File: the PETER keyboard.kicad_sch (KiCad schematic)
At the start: 140 parts

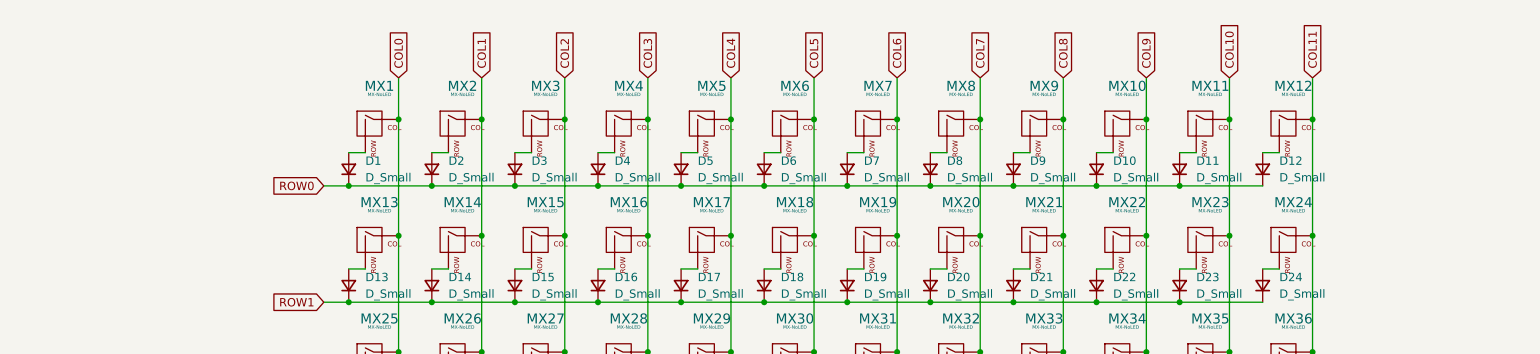
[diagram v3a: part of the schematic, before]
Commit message: added first draft of rotary encoders
not confirmed to work
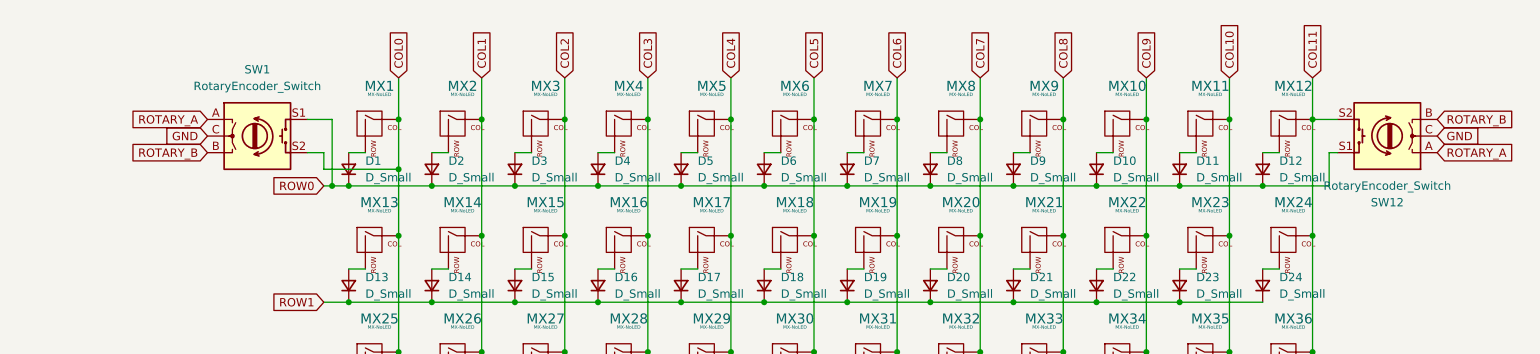
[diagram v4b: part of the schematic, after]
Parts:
- added SW1, SW12: RotaryEncoder_Switch, symbol Device:RotaryEncoder_Switch
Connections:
- net COL0: now also SW1.S2
- net COL11: now also SW12.S2
- net GND: now also SW1.C, SW12.C
- net ROW0: now also SW1.S1, SW12.S1
- new net ROTARY_A: SW1.A, SW12.A
- new net ROTARY_B: SW1.B, SW12.B
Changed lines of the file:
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@@
   (junction (at 240.03 25.4) (diameter 0) (color 0 0 0 0)
   )
+  (junction (at 102.87 35.56) (diameter 0) (color 0 0 0 0)
+  )
   (junction (at 25.4 114.3) (diameter 0) (color 0 0 0 0)
   )
@@
   (junction (at 219.71 106.68) (diameter 0) (color 0 0 0 0)
   )
+  (junction (at 113.03 33.02) (diameter 0) (color 0 0 0 0)
+  )
   (junction (at 105.41 71.12) (diameter 0) (color 0 0 0 0)
   )
@@
   (junction (at 105.41 35.56) (diameter 0) (color 0 0 0 0)
   )
+  (junction (at 245.11 35.56) (diameter 0) (color 0 0 0 0)
+  )
   (junction (at 118.11 53.34) (diameter 0) (color 0 0 0 0)
   )
@@
     (stroke (width 0) (type default) (color 0 0 0 0))
   )
+  (wire (pts (xy 255.27 30.48) (xy 255.27 35.56))
+    (stroke (width 0) (type default) (color 0 0 0 0))
+  )
   (wire (pts (xy 93.98 175.26) (xy 92.71 175.26))
     (stroke (width 0) (type default) (color 0 0 0 0))
@@
     (stroke (width 0) (type default) (color 0 0 0 0))
   )
+  (wire (pts (xy 101.6 30.48) (xy 101.6 33.02))
+    (stroke (width 0) (type default) (color 0 0 0 0))
+  )
   (wire (pts (xy 25.4 119.38) (xy 35.56 119.38))
     (stroke (width 0) (type default) (color 0 0 0 0))
@@
     (stroke (width 0) (type default) (color 0 0 0 0))
   )
+  (wire (pts (xy 102.87 25.4) (xy 102.87 35.56))
+    (stroke (width 0) (type default) (color 0 0 0 0))
+  )
   (wire (pts (xy 118.11 88.9) (xy 130.81 88.9))
     (stroke (width 0) (type default) (color 0 0 0 0))
@@
     (stroke (width 0) (type default) (color 0 0 0 0))
   )
+  (wire (pts (xy 101.6 33.02) (xy 113.03 33.02))
+    (stroke (width 0) (type default) (color 0 0 0 0))
+  )
   (wire (pts (xy 219.71 106.68) (xy 232.41 106.68))
     (stroke (width 0) (type default) (color 0 0 0 0))
@@
     (stroke (width 0) (type default) (color 0 0 0 0))
   )
+  (wire (pts (xy 102.87 35.56) (xy 105.41 35.56))
+    (stroke (width 0) (type default) (color 0 0 0 0))
+  )
   (wire (pts (xy 194.31 48.26) (xy 196.85 48.26))
     (stroke (width 0) (type default) (color 0 0 0 0))
@@
     (stroke (width 0) (type default) (color 0 0 0 0))
   )
+  (wire (pts (xy 113.03 33.02) (xy 113.03 43.18))
+    (stroke (width 0) (type default) (color 0 0 0 0))
+  )
   (wire (pts (xy 214.63 78.74) (xy 214.63 96.52))
     (stroke (width 0) (type default) (color 0 0 0 0))
@@
     (stroke (width 0) (type default) (color 0 0 0 0))
   )
+  (wire (pts (xy 252.73 25.4) (xy 256.54 25.4))
+    (stroke (width 0) (type default) (color 0 0 0 0))
+  )
   (wire (pts (xy 101.6 161.29) (xy 104.14 161.29))
     (stroke (width 0) (type default) (color 0 0 0 0))
@@
     (stroke (width 0) (type default) (color 0 0 0 0))
   )
+  (wire (pts (xy 256.54 30.48) (xy 255.27 30.48))
+    (stroke (width 0) (type default) (color 0 0 0 0))
+  )
   (wire (pts (xy 245.11 48.26) (xy 247.65 48.26))
     (stroke (width 0) (type default) (color 0 0 0 0))
@@
     (stroke (width 0) (type default) (color 0 0 0 0))
   )
-  (wire (pts (xy 101.6 35.56) (xy 105.41 35.56))
+  (wire (pts (xy 101.6 35.56) (xy 102.87 35.56))
     (stroke (width 0) (type default) (color 0 0 0 0))
   )
@@
     (stroke (width 0) (type default) (color 0 0 0 0))
   )
+  (wire (pts (xy 245.11 35.56) (xy 255.27 35.56))
+    (stroke (width 0) (type default) (color 0 0 0 0))
+  )
   (wire (pts (xy 181.61 53.34) (xy 194.31 53.34))
     (stroke (width 0) (type default) (color 0 0 0 0))
@@
     (stroke (width 0) (type default) (color 0 0 0 0))
   )
+  (wire (pts (xy 99.06 30.48) (xy 101.6 30.48))
+    (stroke (width 0) (type default) (color 0 0 0 0))
+  )
   (wire (pts (xy 125.73 43.18) (xy 125.73 60.96))
     (stroke (width 0) (type default) (color 0 0 0 0))
@@
     (stroke (width 0) (type default) (color 0 0 0 0))
   )
-  (wire (pts (xy 113.03 25.4) (xy 113.03 43.18))
+  (wire (pts (xy 113.03 25.4) (xy 113.03 33.02))
     (stroke (width 0) (type default) (color 0 0 0 0))
   )
@@
     (stroke (width 0) (type default) (color 0 0 0 0))
   )
+  (wire (pts (xy 99.06 25.4) (xy 102.87 25.4))
+    (stroke (width 0) (type default) (color 0 0 0 0))
+  )
   (wire (pts (xy 22.86 163.83) (xy 25.4 163.83))
     (stroke (width 0) (type default) (color 0 0 0 0))
@@
     )
   )
+  (global_label "GND" (shape input) (at 271.78 27.94 0) (fields_autoplaced)
+    (effects (font (size 1.27 1.27)) (justify left))
+    (property "Intersheet References" "${INTERSHEET_REFS}" (id 0) (at 278.0636 28.0194 0)
+      (effects (font (size 1.27 1.27)) (justify left) hide)
+    )
+  )
   (global_label "ROW2" (shape input) (at 101.6 71.12 180) (fields_autoplaced)
     (effects (font (size 1.27 1.27)) (justify right))
@@
     )
   )
+  (global_label "ROTARY_A" (shape input) (at 83.82 25.4 180) (fields_autoplaced)
+    (effects (font (size 1.27 1.27)) (justify right))
+    (property "Intersheet References" "${INTERSHEET_REFS}" (id 0) (at 72.3355 25.3206 0)
+      (effects (font (size 1.27 1.27)) (justify right) hide)
+    )
+  )
   (global_label "COL3" (shape input) (at 151.13 19.05 90) (fields_autoplaced)
     (effects (font (size 1.27 1.27)) (justify left))
@@
     )
   )
+  (global_label "GND" (shape input) (at 83.82 27.94 180) (fields_autoplaced)
+    (effects (font (size 1.27 1.27)) (justify right))
+    (property "Intersheet References" "${INTERSHEET_REFS}" (id 0) (at 77.5364 27.8606 0)
+      (effects (font (size 1.27 1.27)) (justify right) hide)
+    )
+  )
   (global_label "COL7" (shape input) (at 201.93 19.05 90) (fields_autoplaced)
     (effects (font (size 1.27 1.27)) (justify left))
@@
     )
   )
+  (global_label "ROTARY_B" (shape input) (at 271.78 25.4 0) (fields_autoplaced)
+    (effects (font (size 1.27 1.27)) (justify left))
+    (property "Intersheet References" "${INTERSHEET_REFS}" (id 0) (at 283.446 25.4794 0)
+      (effects (font (size 1.27 1.27)) (justify left) hide)
+    )
+  )
   (global_label "COL9" (shape input) (at 227.33 19.05 90) (fields_autoplaced)
     (effects (font (size 1.27 1.27)) (justify left))
@@
     )
   )
+  (global_label "ROTARY_B" (shape input) (at 83.82 30.48 180) (fields_autoplaced)
+    (effects (font (size 1.27 1.27)) (justify right))
+    (property "Intersheet References" "${INTERSHEET_REFS}" (id 0) (at 72.154 30.4006 0)
+      (effects (font (size 1.27 1.27)) (justify right) hide)
+    )
+  )
   (global_label "ROW4" (shape input) (at 101.6 106.68 180) (fields_autoplaced)
     (effects (font (size 1.27 1.27)) (justify right))
@@
     )
   )
+  (global_label "ROTARY_A" (shape input) (at 271.78 30.48 0) (fields_autoplaced)
+    (effects (font (size 1.27 1.27)) (justify left))
+    (property "Intersheet References" "${INTERSHEET_REFS}" (id 0) (at 283.2645 30.5594 0)
+      (effects (font (size 1.27 1.27)) (justify left) hide)
+    )
+  )
   (global_label "D+" (shape input) (at 177.8 149.86 0) (fields_autoplaced)
     (effects (font (size 1.27 1.27)) (justify left))
@@
     (pin "1")
   )
+  (symbol (lib_id "Device:RotaryEncoder_Switch") (at 91.44 27.94 0) (unit 1)
+    (in_bom yes) (on_board yes) (fields_autoplaced)
+    (property "Reference" "SW1" (id 0) (at 91.44 17.78 0))
+    (property "Value" "RotaryEncoder_Switch" (id 1) (at 91.44 20.32 0))
+    (property "Footprint" "" (id 2) (at 87.63 23.876 0)
+      (effects (font (size 1.27 1.27)) hide)
+    )
+    (property "Datasheet" "~" (id 3) (at 91.44 21.336 0)
+      (effects (font (size 1.27 1.27)) hide)
+    )
+    (pin "A")
+    (pin "B")
+    (pin "C")
+    (pin "S1")
+    (pin "S2")
+  )
   (symbol (lib_id "MX_Alps_Hybrid:MX-NoLED") (at 248.92 62.23 0) (unit 1)
     (in_bom yes) (on_board yes) (fields_autoplaced)
@@
     (pin "2")
   )
+  (symbol (lib_id "Device:RotaryEncoder_Switch") (at 264.16 27.94 180) (unit 1)
+    (in_bom yes) (on_board yes) (fields_autoplaced)
+    (property "Reference" "SW12" (id 0) (at 264.16 38.1 0))
+    (property "Value" "RotaryEncoder_Switch" (id 1) (at 264.16 35.56 0))
+    (property "Footprint" "" (id 2) (at 267.97 32.004 0)
+      (effects (font (size 1.27 1.27)) hide)
+    )
+    (property "Datasheet" "~" (id 3) (at 264.16 34.544 0)
+      (effects (font (size 1.27 1.27)) hide)
+    )
+    (pin "A")
+    (pin "B")
+    (pin "C")
+    (pin "S1")
+    (pin "S2")
+  )
   (symbol (lib_id "power:GND") (at 20.32 107.95 0) (unit 1)
     (in_bom yes) (on_board yes) (fields_autoplaced)
@@
       (reference "R_reset") (unit 1) (value "10k") (footprint "")
     )
+    (path "/686c98ed-cc3a-4deb-bb9f-69987ce0dea2"
+      (reference "SW1") (unit 1) (value "RotaryEncoder_Switch") (footprint "")
+    )
+    (path "/9508f5e5-418e-4d98-9aec-1f9aa187f8a3"
+      (reference "SW12") (unit 1) (value "RotaryEncoder_Switch") (footprint "")
+    )
     (path "/ec0114a5-eee2-485f-ae5a-b06d664c05d9"

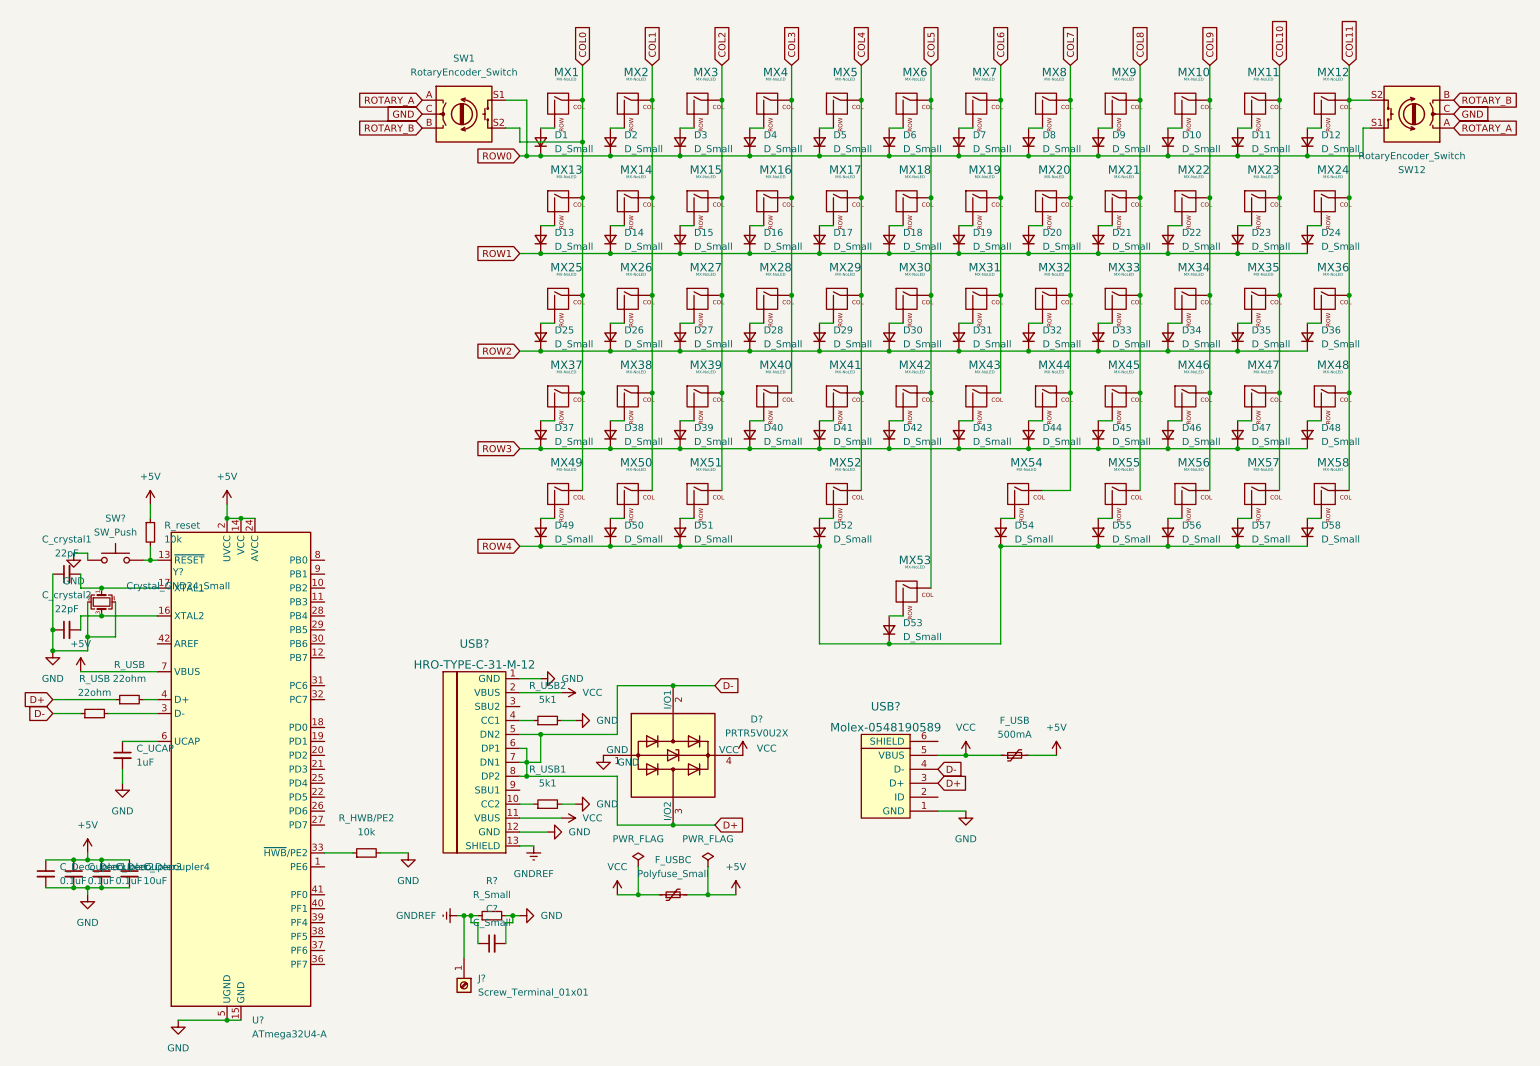
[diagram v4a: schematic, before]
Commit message: USB c cleaned up
older USB port removed
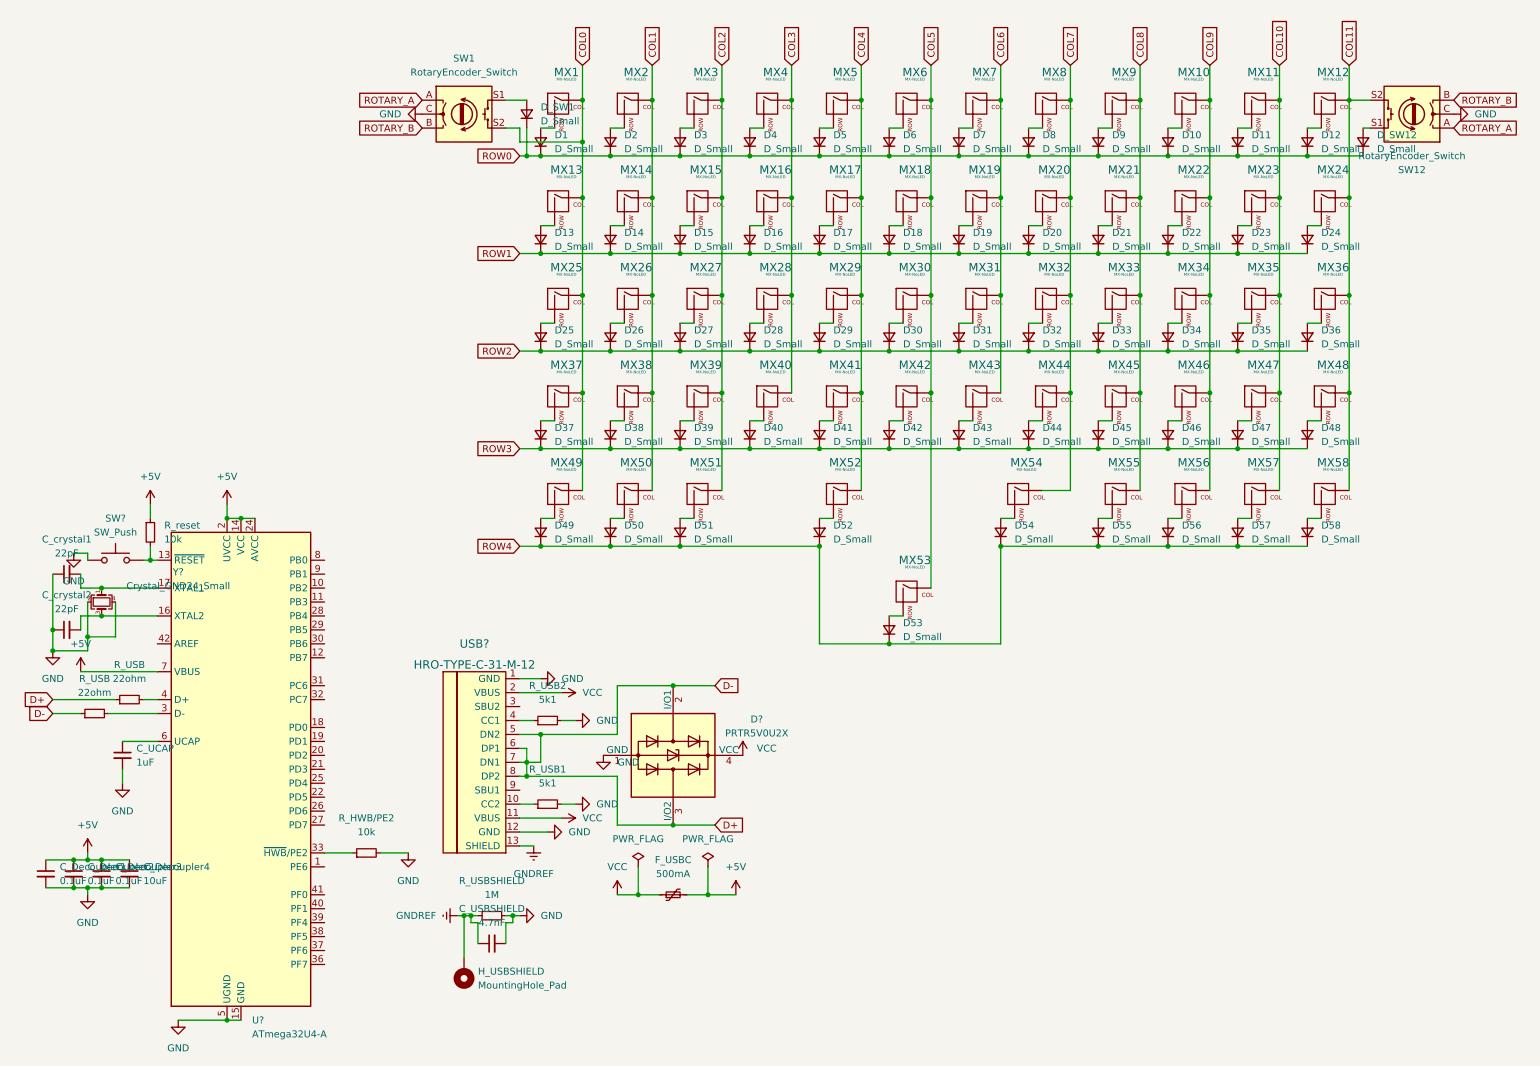
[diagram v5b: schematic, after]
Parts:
- removed F_USB: 500mA, symbol Device:Polyfuse_Small
- removed J?: Screw_Terminal_01x01, symbol Connector:Screw_Terminal_01x01
- removed USB?: Molex-0548190589, symbol random-keyboard-parts:Molex-0548190589
- added D_SW1, D_SW12: D_Small, symbol Device:D_Small
- added H_USBSHIELD: MountingHole_Pad, symbol Mechanical:MountingHole_Pad
- C_USBSHIELD: renamed from C?; value C_Small -> 4.7nF
- F_USBC: value Polyfuse_Small -> 500mA
- R_USBSHIELD: renamed from R?; value R_Small -> 1M
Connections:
- net GNDREF: now also H_USBSHIELD.1
- net ROW0: now also D_SW1.1 (K), D_SW12.1 (K); no longer SW1.S1, SW12.S1
- new net: D_SW12.2 (A), SW12.S1
- new net: D_SW1.2 (A), SW1.S1
